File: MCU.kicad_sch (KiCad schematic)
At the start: 44 parts, among them J15 Conn_01x08, J16 Conn_02x04_Odd_Even, J17 Conn_01x04, J19 Conn_01x04, Q13 BSZ0902NSATMA1, SW1 SW_Push_Dual, SW2 SW_Push_Dual, SW3 SW_DIP_x08, U15 MCP1700-3302E_SOT23, U16 CD74HC4067M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

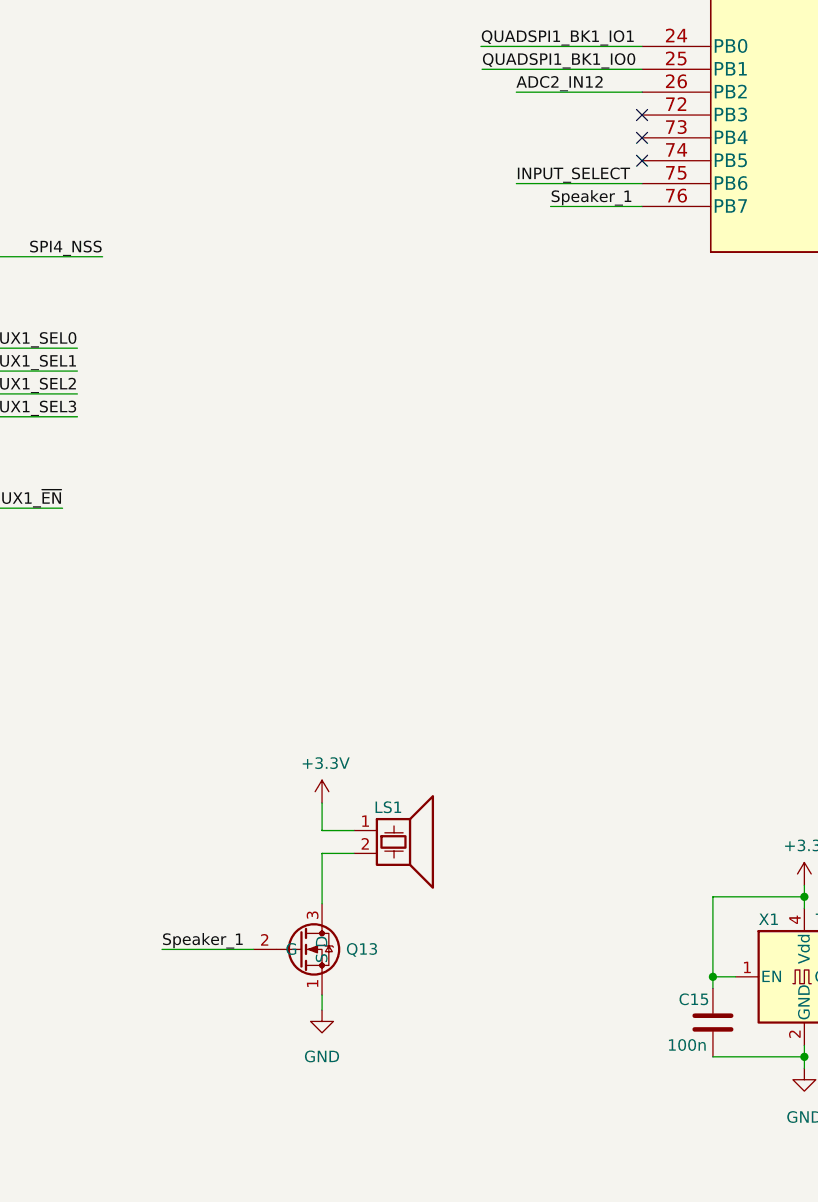
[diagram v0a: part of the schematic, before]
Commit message: Speaker Voltage fixed
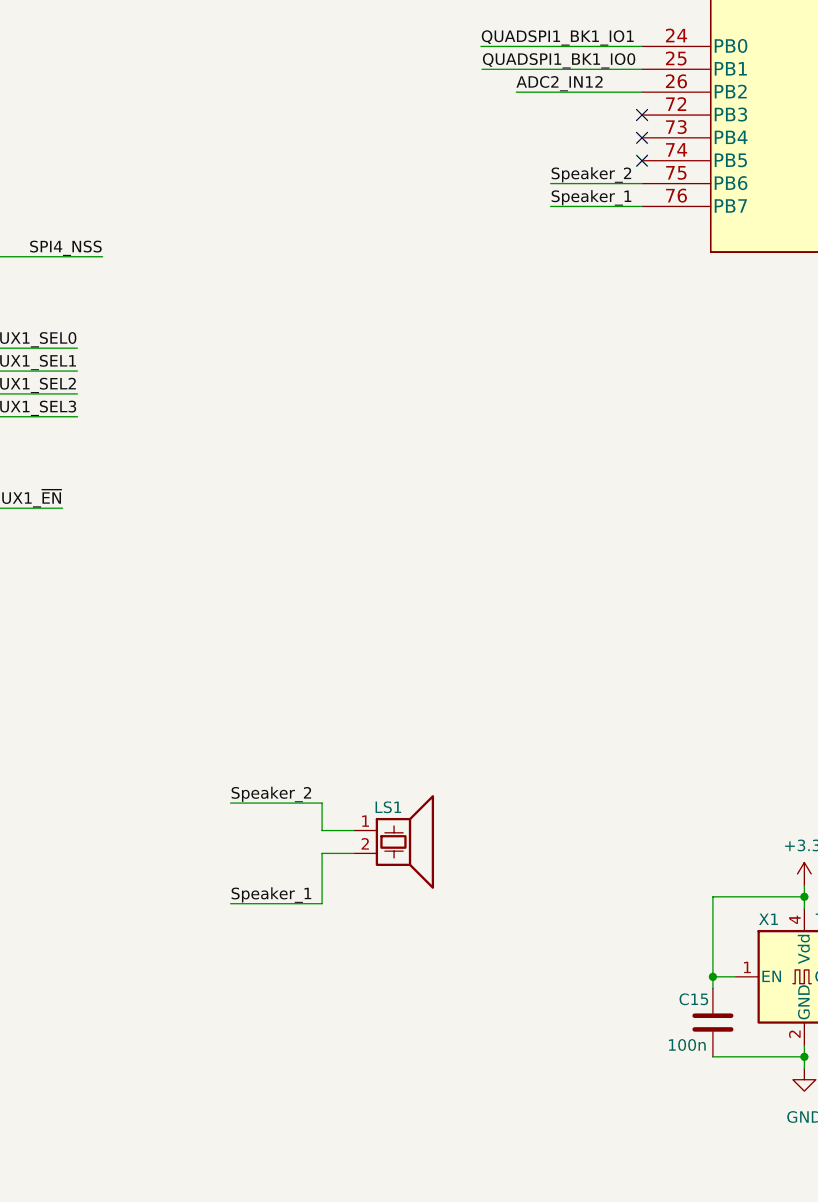
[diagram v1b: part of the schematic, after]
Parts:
- removed Q13: BSZ0902NSATMA1, TXV_Library_Footprints:PG_TSDSON-8, symbol TXV_Library_Symbols:BSZ0902NSATMA1
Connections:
- net +3V3: no longer LS1.1
- net Speaker_1: now also LS1.2
- net INPUT_SELECT renamed Speaker_2
- net Speaker_2: now also LS1.1
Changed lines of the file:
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@@
-    (stroke (width 0) (type default) (color 0 0 0 0))
-  )
-  (wire (pts (xy 245.11 169.672) (xy 231.14 169.672))
     (stroke (width 0) (type default) (color 0 0 0 0))
   )
@@
     (stroke (width 0) (type default) (color 0 0 0 0))
   )
-  (wire (pts (xy 201.93 254.762) (xy 191.77 254.762))
+  (wire (pts (xy 209.55 249.682) (xy 199.39 249.682))
     (stroke (width 0) (type default) (color 0 0 0 0))
   )
@@
     (stroke (width 0) (type default) (color 0 0 0 0))
   )
+  (wire (pts (xy 245.11 169.672) (xy 234.95 169.672))
+    (stroke (width 0) (type default) (color 0 0 0 0))
+  )
   (wire (pts (xy 244.348 66.802) (xy 244.348 57.658))
     (stroke (width 0) (type default) (color 0 0 0 0))
@@
     (stroke (width 0) (type default) (color 0 0 0 0))
   )
-  (wire (pts (xy 209.55 259.842) (xy 209.55 261.493))
-    (stroke (width 0) (type default) (color 0 0 0 0))
-  )
   (wire (pts (xy 316.23 82.042) (xy 327.279 82.042))
     (stroke (width 0) (type default) (color 0 0 0 0))
@@
     (stroke (width 0) (type default) (color 0 0 0 0))
   )
+  (wire (pts (xy 209.55 238.506) (xy 199.39 238.506))
+    (stroke (width 0) (type default) (color 0 0 0 0))
+  )
   (wire (pts (xy 334.01 74.422) (xy 316.23 74.422))
     (stroke (width 0) (type default) (color 0 0 0 0))
@@
     (effects (font (size 1.27 1.27)) (justify left bottom))
   )
+  (label "Speaker_2" (at 199.39 238.506 0)
+    (effects (font (size 1.27 1.27)) (justify left bottom))
+  )
   (label "MUX1_SEL0" (at 182.372 187.96 180)
     (effects (font (size 1.27 1.27)) (justify right bottom))
@@
     (effects (font (size 1.27 1.27)) (justify left bottom))
   )
-  (label "Speaker_1" (at 191.77 254.762 0)
+  (label "Speaker_1" (at 199.39 249.682 0)
     (effects (font (size 1.27 1.27)) (justify left bottom))
   )
@@
     (effects (font (size 1.27 1.27)) (justify left bottom))
   )
+  (label "Speaker_2" (at 234.95 169.672 0)
+    (effects (font (size 1.27 1.27)) (justify left bottom))
+  )
   (label "CANH1" (at 46.736 196.088 0)
     (effects (font (size 1.27 1.27)) (justify left bottom))
@@
   (label "SPI4_MOSI" (at 330.2 172.212 180)
     (effects (font (size 1.27 1.27)) (justify right bottom))
-  )
-  (label "INPUT_SELECT" (at 231.14 169.672 0)
-    (effects (font (size 1.27 1.27)) (justify left bottom))
   )
   (hierarchical_label "ANALOG_IN_12" (shape input) (at 386.588 82.804 0)
@@
     (pin "2")
   )
-  (symbol (lib_id "TXV_Library_Symbols:BSZ0902NSATMA1") (at 208.28 254.762 0) (unit 1)
-    (in_bom yes) (on_board yes)
-    (property "Reference" "Q13" (id 0) (at 212.217 254.762 0)
-      (effects (font (size 1.27 1.27)) (justify left))
-    )
-    (property "Value" "BSZ0902NSATMA1" (id 1) (at 212.1916 255.905 0)
-      (effects (font (size 1.27 1.27)) (justify left) hide)
-    )
-    (property "Footprint" "TXV_Library_Footprints:PG_TSDSON-8" (id 2) (at 208.28 254.762 0)
-      (effects (font (size 1.27 1.27)) hide)
-    )
-    (property "Datasheet" "" (id 3) (at 208.28 254.762 0)
-      (effects (font (size 1.27 1.27)) hide)
-    )
-    (pin "1")
-    (pin "2")
-    (pin "3")
-  )
   (symbol (lib_id "Connector:TestPoint") (at 241.173 75.692 0) (unit 1)
     (in_bom yes) (on_board yes)
@@
     )
     (property "Datasheet" "" (id 3) (at 158.496 218.44 0)
-      (effects (font (size 1.27 1.27)) hide)
-    )
-    (pin "1")
-  )
-  (symbol (lib_id "power:GND") (at 209.55 261.493 0) (unit 1)
-    (in_bom yes) (on_board yes) (fields_autoplaced)
-    (property "Reference" "#PWR0142" (id 0) (at 209.55 267.843 0)
-      (effects (font (size 1.27 1.27)) hide)
-    )
-    (property "Value" "GND" (id 1) (at 209.55 266.7 0))
-    (property "Footprint" "" (id 2) (at 209.55 261.493 0)
-      (effects (font (size 1.27 1.27)) hide)
-    )
-    (property "Datasheet" "" (id 3) (at 209.55 261.493 0)
       (effects (font (size 1.27 1.27)) hide)
     )
@@
     )
     (property "Datasheet" "" (id 3) (at 125.476 213.614 0)
-      (effects (font (size 1.27 1.27)) hide)
-    )
-    (pin "1")
-  )
-  (symbol (lib_id "power:+3.3V") (at 209.55 238.506 0) (unit 1)
-    (in_bom yes) (on_board yes)
-    (property "Reference" "#PWR0141" (id 0) (at 209.55 242.316 0)
-      (effects (font (size 1.27 1.27)) hide)
-    )
-    (property "Value" "+3.3V" (id 1) (at 209.931 234.1118 0))
-    (property "Footprint" "" (id 2) (at 209.55 238.506 0)
-      (effects (font (size 1.27 1.27)) hide)
-    )
-    (property "Datasheet" "" (id 3) (at 209.55 238.506 0)
       (effects (font (size 1.27 1.27)) hide)
     )
@@
       (effects (font (size 1.27 1.27)) hide)
     )
-    (property "Datasheet" "~" (id 3) (at 217.297 242.824 0)
-      (effects (font (size 1.27 1.27)) hide)
-    )
+    (property "Datasheet" "https://docs.rs-online.com/d315/0900766b81465df1.pdf" (id 3) (at 217.297 242.824 0)
+      (effects (font (size 1.27 1.27)) hide)
+    )

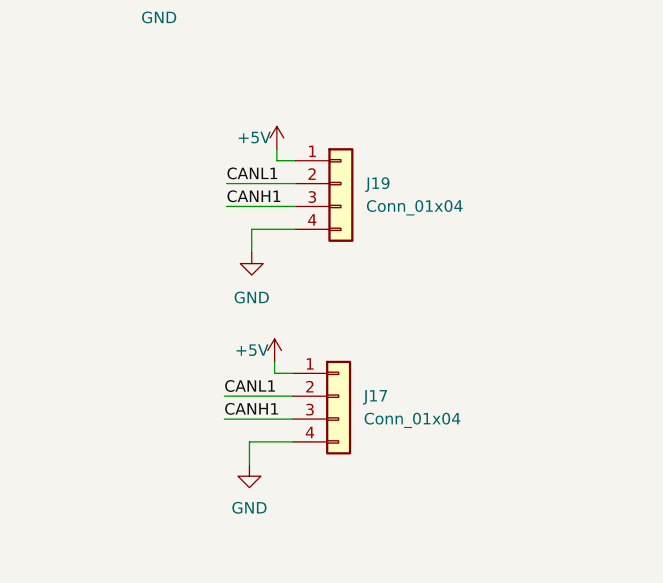
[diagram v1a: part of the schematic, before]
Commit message: Can connector pinout fix
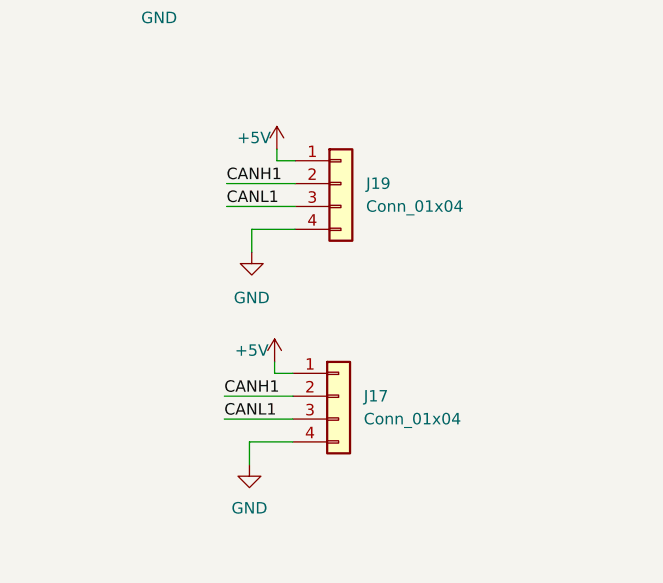
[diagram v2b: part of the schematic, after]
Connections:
- net CANH1: now also J17.2 (Pin_2), J19.2 (Pin_2); no longer J17.3 (Pin_3), J19.3 (Pin_3)
- net CANL1: now also J17.3 (Pin_3), J19.3 (Pin_3); no longer J17.2 (Pin_2), J19.2 (Pin_2)
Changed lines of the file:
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@@
     (effects (font (size 1.27 1.27)) (justify left bottom))
   )
-  (label "CANH1" (at 46.482 219.71 0)
+  (label "CANL1" (at 46.482 219.71 0)
     (effects (font (size 1.27 1.27)) (justify left bottom))
   )
@@
     (effects (font (size 1.27 1.27)) (justify left bottom))
   )
-  (label "CANL1" (at 46.482 217.17 0)
+  (label "CANH1" (at 46.482 217.17 0)
     (effects (font (size 1.27 1.27)) (justify left bottom))
   )
@@
     (effects (font (size 1.27 1.27)) (justify left bottom))
   )
-  (label "CANH1" (at 46.736 196.088 0)
+  (label "CANL1" (at 46.736 196.088 0)
     (effects (font (size 1.27 1.27)) (justify left bottom))
   )
@@
     (effects (font (size 1.27 1.27)) (justify left bottom))
   )
-  (label "CANL1" (at 46.736 193.548 0)
-    (effects (font (size 1.27 1.27)) (justify left bottom))
-  )
+  (label "CANH1" (at 46.736 193.548 0)
+    (effects (font (size 1.27 1.27)) (justify left bottom))
+  )

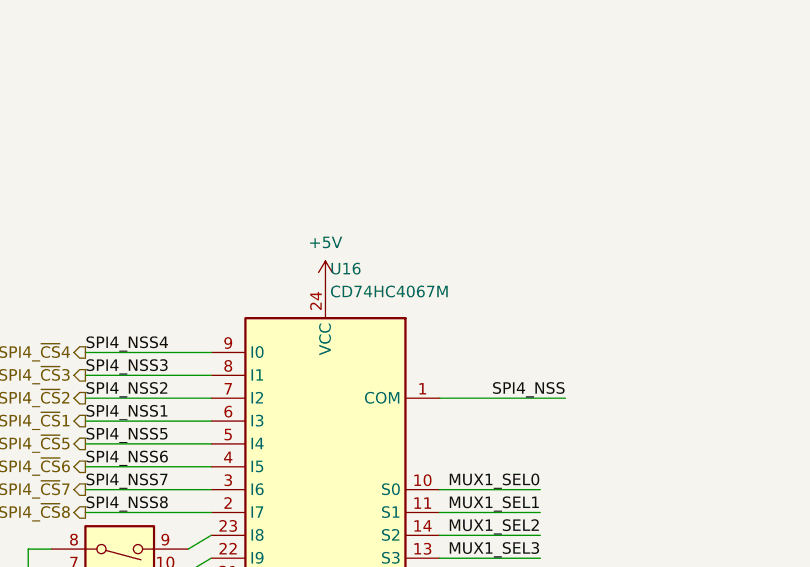
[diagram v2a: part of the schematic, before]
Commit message: Correct MUX Footprint added
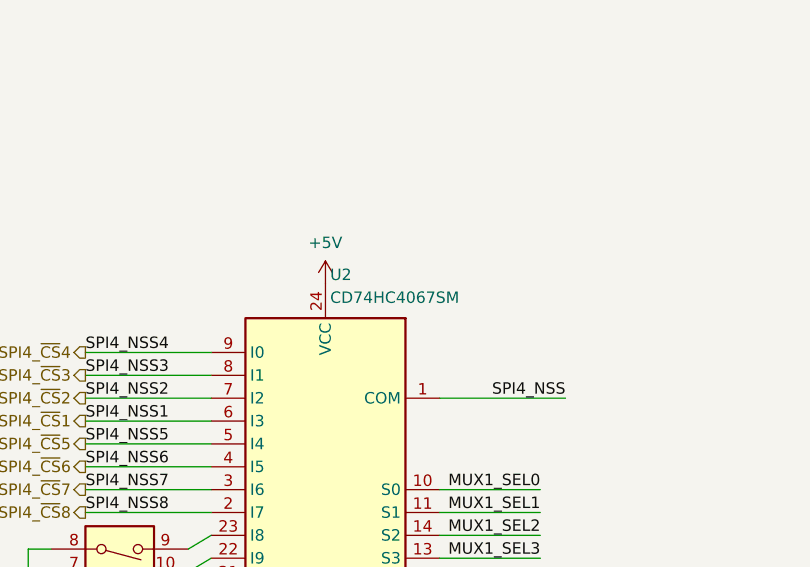
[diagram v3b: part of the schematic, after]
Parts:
- removed U16: CD74HC4067M, Package_SO:SOIC-24W_7.5x15.4mm_P1.27mm, symbol 74xx:CD74HC4067M
- added U2: CD74HC4067SM, Package_SO:SSOP-24_5.3x8.2mm_P0.65mm, symbol 74xx:CD74HC4067SM
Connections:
- net +5V: now also U2.24 (VCC)
- net GND: now also U2.12 (GND)
- net MUX1_SEL0: now also U2.10 (S0)
- net MUX1_SEL1: now also U2.11 (S1)
- net MUX1_SEL2: now also U2.14 (S2)
- net MUX1_SEL3: now also U2.13 (S3)
- net MUX1_~{EN}: now also U2.15 (~{E})
- net SPI4_NSS: now also U2.1 (COM)
- net SPI4_~{CS}1: now also U2.6 (I3)
- net SPI4_~{CS}2: now also U2.7 (I2)
- net SPI4_~{CS}3: now also U2.8 (I1)
- net SPI4_~{CS}4: now also U2.9 (I0)
- net SPI4_~{CS}5: now also U2.5 (I4)
- net SPI4_~{CS}6: now also U2.4 (I5)
- net SPI4_~{CS}7: now also U2.3 (I6)
- net SPI4_~{CS}8: now also U2.2 (I7)
- net at SW3.10: now also U2.22 (I9)
- net at SW3.11: now also U2.21 (I10)
- net at SW3.12: now also U2.20 (I11)
- net at SW3.13: now also U2.19 (I12)
- net at SW3.14: now also U2.18 (I13)
- net at SW3.15: now also U2.17 (I14)
- net at SW3.16: now also U2.16 (I15)
- net at SW3.9: now also U2.23 (I8)

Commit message: WIP
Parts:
- removed TP5: TestPoint, TestPoint:TestPoint_THTPad_D1.0mm_Drill0.5mm, symbol Connector:TestPoint
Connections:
- net ANALOG_IN_1: now also U19.57 (PA9); no longer U19.56 (PA8)
- net BUTTON_1: now also U19.53 (PC7); no longer U19.54 (PC8)
- net En1: now also U19.58 (PA10); no longer U19.57 (PA9)
- net En2: now also U19.54 (PC8); no longer U19.55 (PC9)
- net En4: now also U19.65 (PA15); no longer U19.58 (PA10)
- net SPI4_~{CS}6: now also U2.2 (I7); no longer U2.4 (I5)
- net SPI4_~{CS}7: now also U2.4 (I5); no longer U2.3 (I6)
- net SPI4_~{CS}8: now also U2.3 (I6); no longer U2.2 (I7)
- net Speaker_1: now also U19.55 (PC9); no longer U19.76 (PB7)
- net Speaker_2: now also U19.56 (PA8); no longer U19.75 (PB6)
- no-connect marks 11 -> 12

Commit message: WIP
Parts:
- removed TP6: TestPoint, TestPoint:TestPoint_THTPad_D1.0mm_Drill0.5mm, symbol Connector:TestPoint
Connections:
- net ANALOG_IN_10: now also U19.9 (PC1); no longer U19.17 (PA3)
- net ANALOG_IN_11: now also U19.11 (PC3); no longer U19.13 (PA1)
- net ANALOG_IN_12: now also U19.22 (PC4); no longer U19.23 (PC5)
- net ANALOG_IN_7: now also U19.8 (PC0); no longer U19.12 (PA0)
- net ANALOG_IN_8: now also U19.17 (PA3); no longer U19.10 (PC2)
- net ANALOG_IN_9: now also U19.23 (PC5); no longer U19.22 (PC4)
- net En11: now also U19.10 (PC2); no longer U19.11 (PC3)
- net En12: now also U19.12 (PA0); no longer U19.9 (PC1)
- net En8: now also U19.13 (PA1); no longer U19.8 (PC0)
- no-connect marks 12 -> 13
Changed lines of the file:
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@@
   (no_connect (at 245.11 88.392))
   (no_connect (at 245.11 97.282))
+  (no_connect (at 316.23 126.492))
   (no_connect (at 58.293 85.979))
   (wire (pts (xy 49.403 157.607) (xy 51.943 157.607))
@@
     (effects (font (size 1.27 1.27)) (justify right bottom))
   )
-  (label "ADC1_IN2" (at 372.618 80.391 0)
+  (label "ADC12_IN9" (at 372.618 80.391 0)
     (effects (font (size 1.27 1.27)) (justify left bottom))
   )
@@
     (effects (font (size 1.27 1.27)) (justify right bottom))
   )
-  (label "ADC1_IN8" (at 372.618 72.771 0)
+  (label "ADC1_IN4" (at 372.618 72.771 0)
     (effects (font (size 1.27 1.27)) (justify left bottom))
   )
@@
     (effects (font (size 1.27 1.27)) (justify right bottom))
   )
-  (label "En8" (at 330.2 93.472 180)
-    (effects (font (size 1.27 1.27)) (justify right bottom))
-  )
-  (label "ADC1_IN4" (at 372.618 77.851 0)
+  (label "ADC12_IN6" (at 330.2 93.472 180)
+    (effects (font (size 1.27 1.27)) (justify right bottom))
+  )
+  (label "ADC12_IN7" (at 372.618 77.851 0)
     (effects (font (size 1.27 1.27)) (justify left bottom))
   )
@@
     (effects (font (size 1.27 1.27)) (justify left bottom))
   )
-  (label "ADC1_IN1" (at 231.14 108.712 0)
+  (label "En12" (at 231.14 108.712 0)
     (effects (font (size 1.27 1.27)) (justify left bottom))
   )
@@
     (effects (font (size 1.27 1.27)) (justify right bottom))
   )
-  (label "ADC1_IN8" (at 330.2 98.552 180)
+  (label "En11" (at 330.2 98.552 180)
     (effects (font (size 1.27 1.27)) (justify right bottom))
   )
@@
     (effects (font (size 1.27 1.27)) (justify right bottom))
   )
-  (label "ADC2_IN11" (at 372.618 82.804 0)
+  (label "ADC2_IN5" (at 372.618 82.804 0)
     (effects (font (size 1.27 1.27)) (justify left bottom))
   )
@@
     (effects (font (size 1.27 1.27)) (justify right bottom))
   )
-  (label "ADC1_IN2" (at 231.14 111.252 0)
+  (label "En8" (at 231.14 111.252 0)
     (effects (font (size 1.27 1.27)) (justify left bottom))
   )
@@
     (effects (font (size 1.27 1.27)) (justify left bottom))
   )
-  (label "En11" (at 330.2 101.092 180)
+  (label "ADC12_IN9" (at 330.2 101.092 180)
     (effects (font (size 1.27 1.27)) (justify right bottom))
   )
@@
     (effects (font (size 1.27 1.27)) (justify left bottom))
   )
-  (label "ADC2_IN5" (at 372.618 75.311 0)
+  (label "ADC2_IN11" (at 372.618 75.311 0)
     (effects (font (size 1.27 1.27)) (justify left bottom))
   )
@@
     (effects (font (size 1.27 1.27)) (justify right bottom))
   )
-  (label "En12" (at 330.2 96.012 180)
-    (effects (font (size 1.27 1.27)) (justify right bottom))
-  )
-  (label "ADC1_IN1" (at 372.618 70.231 0)
+  (label "ADC12_IN7" (at 330.2 96.012 180)
+    (effects (font (size 1.27 1.27)) (justify right bottom))
+  )
+  (label "ADC12_IN6" (at 372.618 70.231 0)
     (effects (font (size 1.27 1.27)) (justify left bottom))
   )
@@
     (pin "2")
   )
-  (symbol (lib_id "Connector:TestPoint") (at 316.23 126.492 270) (unit 1)
-    (in_bom yes) (on_board yes)
-    (property "Reference" "TP6" (id 0) (at 321.31 126.492 90)
-      (effects (font (size 1.27 1.27)) (justify left))
-    )
-    (property "Value" "TestPoint" (id 1) (at 319.2018 125.0188 0)
-      (effects (font (size 1.27 1.27)) (justify right) hide)
-    )
-    (property "Footprint" "TestPoint:TestPoint_THTPad_D1.0mm_Drill0.5mm" (id 2) (at 316.23 131.572 0)
-      (effects (font (size 1.27 1.27)) hide)
-    )
-    (property "Datasheet" "~" (id 3) (at 316.23 131.572 0)
-      (effects (font (size 1.27 1.27)) hide)
-    )
-    (pin "1")
-  )
   (symbol (lib_id "Switch:SW_Push") (at 46.736 54.864 0) (unit 1)

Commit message: WIP
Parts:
- removed TP4: TestPoint, TestPoint:TestPoint_THTPad_D1.0mm_Drill0.5mm, symbol Connector:TestPoint
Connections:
- no-connect marks 13 -> 14
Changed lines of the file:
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@@
   (no_connect (at 245.11 167.132))
   (no_connect (at 128.143 269.875))
+  (no_connect (at 316.23 71.882))
   (no_connect (at 47.625 123.825))
   (no_connect (at 245.11 169.672))
@@
       (effects (font (size 1.27 1.27)) hide)
     )
-    (pin "1")
-  )
-  (symbol (lib_id "Connector:TestPoint") (at 316.23 71.882 270) (unit 1)
-    (in_bom yes) (on_board yes)
-    (property "Reference" "TP4" (id 0) (at 321.31 71.247 90)
-      (effects (font (size 1.27 1.27)) (justify left))
-    )
-    (property "Value" "TestPoint" (id 1) (at 319.2018 70.4088 0)
-      (effects (font (size 1.27 1.27)) (justify right) hide)
-    )
-    (property "Footprint" "TestPoint:TestPoint_THTPad_D1.0mm_Drill0.5mm" (id 2) (at 316.23 76.962 0)
-      (effects (font (size 1.27 1.27)) hide)
-    )
-    (property "Datasheet" "~" (id 3) (at 316.23 76.962 0)
-      (effects (font (size 1.27 1.27)) hide)
-    )
